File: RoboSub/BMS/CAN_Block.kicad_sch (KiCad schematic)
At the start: 3 parts, among them U2 TCAN330G

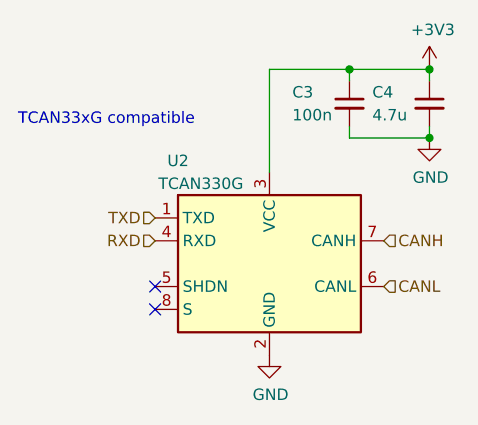
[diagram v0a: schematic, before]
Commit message: cleaned up schematic
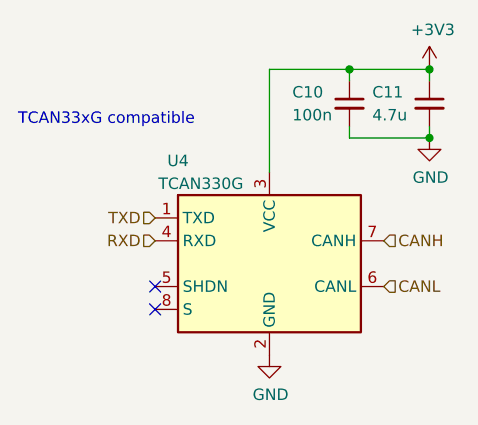
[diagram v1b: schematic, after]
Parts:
- renumbered C3 to C10, C4 to C11, U2 to U4
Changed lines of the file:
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@@
   (symbol (lib_id "Device:C_Small") (at 158.75 86.36 0) (unit 1)
     (in_bom yes) (on_board yes)
-    (property "Reference" "C3" (id 0) (at 152.4 85.09 0)
+    (property "Reference" "C10" (id 0) (at 152.4 85.09 0)
       (effects (font (size 1.27 1.27)) (justify left))
     )
@@
   (symbol (lib_id "Device:C_Small") (at 167.64 86.36 0) (unit 1)
     (in_bom yes) (on_board yes)
-    (property "Reference" "C4" (id 0) (at 161.29 85.09 0)
+    (property "Reference" "C11" (id 0) (at 161.29 85.09 0)
       (effects (font (size 1.27 1.27)) (justify left))
     )
@@
   (symbol (lib_id "Interface_CAN_LIN:TCAN330G") (at 149.86 104.14 0) (unit 1)
     (in_bom yes) (on_board yes)
-    (property "Reference" "U2" (id 0) (at 139.7 92.71 0))
+    (property "Reference" "U4" (id 0) (at 139.7 92.71 0))
     (property "Value" "TCAN330G" (id 1) (at 142.24 95.25 0))
     (property "Footprint" "Package_SO:SOIC-8_3.9x4.9mm_P1.27mm" (id 2) (at 149.86 116.84 0)
@@
   (symbol (lib_id "power:+3V3") (at 167.64 82.55 0) (unit 1)
     (in_bom yes) (on_board yes)
-    (property "Reference" "#PWR020" (id 0) (at 167.64 86.36 0)
+    (property "Reference" "#PWR033" (id 0) (at 167.64 86.36 0)
       (effects (font (size 1.27 1.27)) hide)
     )
@@
   (symbol (lib_id "power:GND") (at 149.86 114.3 0) (unit 1)
     (in_bom yes) (on_board yes)
-    (property "Reference" "#PWR019" (id 0) (at 149.86 120.65 0)
+    (property "Reference" "#PWR032" (id 0) (at 149.86 120.65 0)
       (effects (font (size 1.27 1.27)) hide)
     )
@@
   (symbol (lib_id "power:GND") (at 167.64 90.17 0) (unit 1)
     (in_bom yes) (on_board yes)
-    (property "Reference" "#PWR021" (id 0) (at 167.64 96.52 0)
+    (property "Reference" "#PWR034" (id 0) (at 167.64 96.52 0)
       (effects (font (size 1.27 1.27)) hide)
     )
